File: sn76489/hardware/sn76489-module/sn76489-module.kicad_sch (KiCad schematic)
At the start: 12 parts

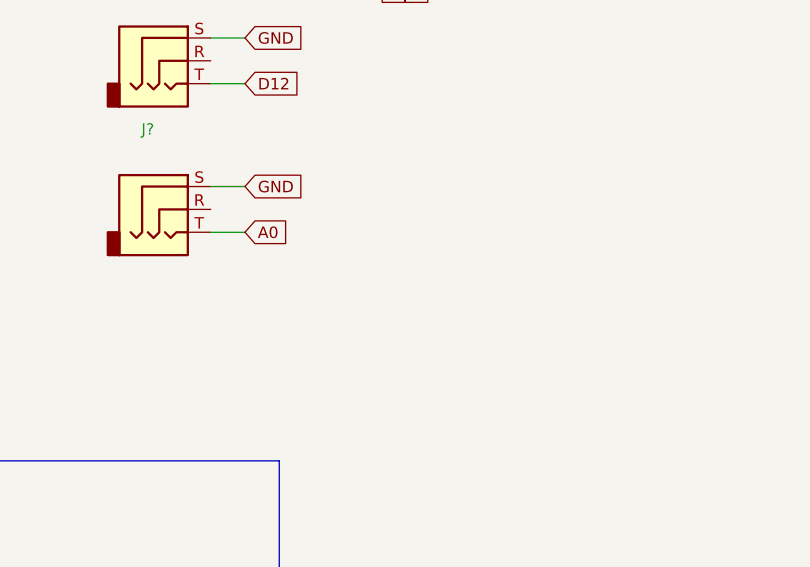
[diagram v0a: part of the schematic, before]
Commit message: updated to add v/oct resistors/caps
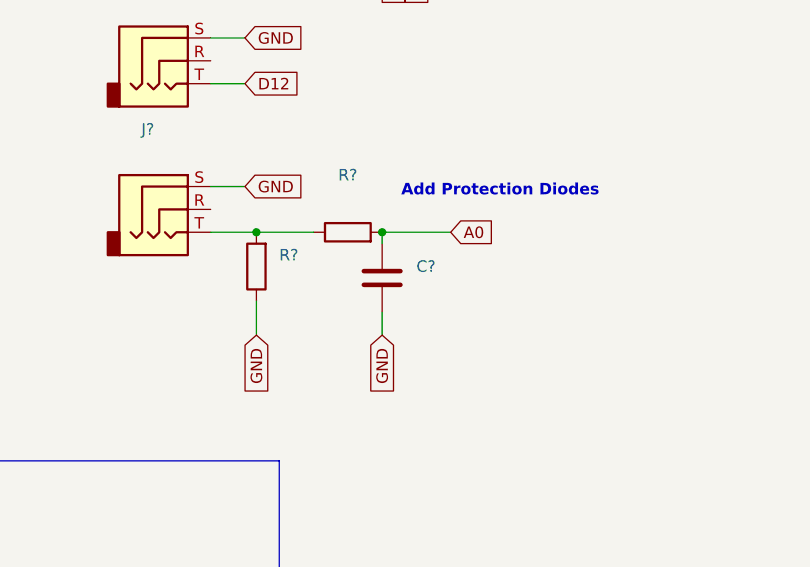
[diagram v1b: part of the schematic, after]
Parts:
- added C?: (no value), symbol Device:C
- added R? (x2): (no value), symbol Device:R
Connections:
- net A0: now also C?.1, R?.2; no longer J?.T
- net GND: now also C?.2, R?.1
- new net: J?.T, R?.1, R?.2
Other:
- note added: "Add Protection Diodes"
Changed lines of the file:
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@@
 (kicad_sch (version 20211123) (generator eeschema)
   (paper "A4")
+  (junction (at 113.03 120.65) (diameter 0) (color 0 0 0 0)
+  )
   (junction (at 36.83 34.29) (diameter 0) (color 0 0 0 0)
   )
@@
   (junction (at 24.13 36.83) (diameter 0) (color 0 0 0 0)
   )
+  (junction (at 99.06 120.65) (diameter 0) (color 0 0 0 0)
+  )
   (junction (at 24.13 41.91) (diameter 0) (color 0 0 0 0)
   )
@@
     (stroke (width 0) (type default) (color 0 0 0 0))
   )
+  (wire (pts (xy 113.03 129.54) (xy 113.03 132.08))
+    (stroke (width 0) (type default) (color 0 0 0 0))
+  )
   (wire (pts (xy 59.69 161.29) (xy 59.69 168.91))
     (stroke (width 0) (type default) (color 0 0 0 0))
@@
     (stroke (width 0) (type default) (color 0 0 0 0))
   )
+  (wire (pts (xy 99.06 120.65) (xy 105.41 120.65))
+    (stroke (width 0) (type default) (color 0 0 0 0))
+  )
   (wire (pts (xy 21.59 41.91) (xy 24.13 41.91))
     (stroke (width 0) (type default) (color 0 0 0 0))
@@
     (stroke (width 0) (type default) (color 0 0 0 0))
   )
-  (wire (pts (xy 93.98 120.65) (xy 97.79 120.65))
+  (wire (pts (xy 113.03 120.65) (xy 120.65 120.65))
     (stroke (width 0) (type default) (color 0 0 0 0))
   )
@@
     (stroke (width 0) (type default) (color 0 0 0 0))
   )
+  (wire (pts (xy 93.98 120.65) (xy 99.06 120.65))
+    (stroke (width 0) (type default) (color 0 0 0 0))
+  )
   (wire (pts (xy 38.1 62.23) (xy 39.37 62.23))
     (stroke (width 0) (type default) (color 0 0 0 0))
@@
     (stroke (width 0) (type default) (color 0 0 0 0))
   )
+  (wire (pts (xy 113.03 120.65) (xy 113.03 121.92))
+    (stroke (width 0) (type default) (color 0 0 0 0))
+  )
   (wire (pts (xy 80.01 50.8) (xy 101.6 50.8))
     (stroke (width 0) (type default) (color 0 0 0 0))
@@
     (stroke (width 0) (type default) (color 0 0 0 0))
   )
+  (wire (pts (xy 99.06 128.27) (xy 99.06 132.08))
+    (stroke (width 0) (type default) (color 0 0 0 0))
+  )
   (wire (pts (xy 80.01 66.04) (xy 101.6 66.04))
     (stroke (width 0) (type default) (color 0 0 0 0))
@@
   (wire (pts (xy 93.98 115.57) (xy 97.79 115.57))
     (stroke (width 0) (type default) (color 0 0 0 0))
+  )
+  (text "Add Protection Diodes" (at 137.16 116.84 180)
+    (effects (font (size 1.27 1.27) (thickness 0.254) bold) (justify right bottom))
   )
   (text "Audio Out (TL072)" (at 62.23 144.78 180)
@@
     )
   )
+  (global_label "GND" (shape input) (at 99.06 132.08 270) (fields_autoplaced)
+    (effects (font (size 1.27 1.27)) (justify right))
+    (property "Intersheet References" "${INTERSHEET_REFS}" (id 0) (at 99.1394 138.3636 90)
+      (effects (font (size 1.27 1.27)) (justify right) hide)
+    )
+  )
   (global_label "-12" (shape input) (at 21.59 41.91 180) (fields_autoplaced)
     (effects (font (size 1.27 1.27)) (justify right))
@@
     )
   )
-  (global_label "A0" (shape input) (at 97.79 120.65 0) (fields_autoplaced)
-    (effects (font (size 1.27 1.27)) (justify left))
-    (property "Intersheet References" "${INTERSHEET_REFS}" (id 0) (at 102.5012 120.5706 0)
+  (global_label "GND" (shape input) (at 113.03 132.08 270) (fields_autoplaced)
+    (effects (font (size 1.27 1.27)) (justify right))
+    (property "Intersheet References" "${INTERSHEET_REFS}" (id 0) (at 113.1094 138.3636 90)
+      (effects (font (size 1.27 1.27)) (justify right) hide)
+    )
+  )
+  (global_label "A0" (shape input) (at 120.65 120.65 0) (fields_autoplaced)
+    (effects (font (size 1.27 1.27)) (justify left))
+    (property "Intersheet References" "${INTERSHEET_REFS}" (id 0) (at 125.3612 120.5706 0)
       (effects (font (size 1.27 1.27)) (justify left) hide)
     )
@@
     (pin "8")
   )
+  (symbol (lib_id "Device:C") (at 113.03 125.73 0) (unit 1)
+    (in_bom yes) (on_board yes) (fields_autoplaced)
+    (property "Reference" "C?" (id 0) (at 116.84 124.4599 0)
+      (effects (font (size 1.27 1.27)) (justify left))
+    )
+    (property "Value" "" (id 1) (at 116.84 126.9999 0)
+      (effects (font (size 1.27 1.27)) (justify left))
+    )
+    (property "Footprint" "" (id 2) (at 113.9952 129.54 0)
+      (effects (font (size 1.27 1.27)) hide)
+    )
+    (property "Datasheet" "~" (id 3) (at 113.03 125.73 0)
+      (effects (font (size 1.27 1.27)) hide)
+    )
+    (pin "1")
+    (pin "2")
+  )
   (symbol (lib_id "Oscillator:ACO-xxxMHz") (at 30.48 96.52 0) (unit 1)
     (in_bom yes) (on_board yes) (fields_autoplaced)
@@
     (pin "S")
     (pin "T")
+  )
+  (symbol (lib_id "Device:R") (at 99.06 124.46 180) (unit 1)
+    (in_bom yes) (on_board yes) (fields_autoplaced)
+    (property "Reference" "R?" (id 0) (at 101.6 123.1899 0)
+      (effects (font (size 1.27 1.27)) (justify right))
+    )
+    (property "Value" "" (id 1) (at 101.6 125.7299 0)
+      (effects (font (size 1.27 1.27)) (justify right))
+    )
+    (property "Footprint" "" (id 2) (at 100.838 124.46 90)
+      (effects (font (size 1.27 1.27)) hide)
+    )
+    (property "Datasheet" "~" (id 3) (at 99.06 124.46 0)
+      (effects (font (size 1.27 1.27)) hide)
+    )
+    (pin "1")
+    (pin "2")
   )
   (symbol (lib_id "zoul0813:SN76489") (at 69.85 60.96 0) (unit 1)
@@
     (pin "9")
   )
+  (symbol (lib_id "Device:R") (at 109.22 120.65 90) (unit 1)
+    (in_bom yes) (on_board yes) (fields_autoplaced)
+    (property "Reference" "R?" (id 0) (at 109.22 114.3 90))
+    (property "Value" "" (id 1) (at 109.22 116.84 90))
+    (property "Footprint" "" (id 2) (at 109.22 122.428 90)
+      (effects (font (size 1.27 1.27)) hide)
+    )
+    (property "Datasheet" "~" (id 3) (at 109.22 120.65 0)
+      (effects (font (size 1.27 1.27)) hide)
+    )
+    (pin "1")
+    (pin "2")
+  )
   (sheet_instances
     (path "/" (page "1"))
@@
       (reference "A?") (unit 1) (value "Arduino_Nano_v3.x") (footprint "Module:Arduino_Nano")
     )
+    (path "/4d859526-a1e4-4cae-bd63-00dc40c4011d"
+      (reference "C?") (unit 1) (value "47nF") (footprint "")
+    )
     (path "/29a57ba1-85ea-482c-9a07-df5843a7cf25"
       (reference "J?") (unit 1) (value "Gate In") (footprint "Norlin's Library:Jack_3.5mm_Nine_to_Nine_Vertical")
@@
       (reference "J?") (unit 1) (value "V/OCT In") (footprint "Norlin's Library:Jack_3.5mm_Nine_to_Nine_Vertical")
     )
+    (path "/cf6e2b6b-16f5-46a3-ab08-d34fc05baa11"
+      (reference "R?") (unit 1) (value "100k") (footprint "")
+    )
+    (path "/eff474b3-d5e0-4718-853b-f939fd805282"
+      (reference "R?") (unit 1) (value "100") (footprint "")
+    )
     (path "/29bb7297-26fb-4776-9266-2355d022bab0"
